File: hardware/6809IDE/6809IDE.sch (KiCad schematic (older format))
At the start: 5 parts, among them J1 SS50-LIKE, J2 ATA-IDE, J3 Conn_01x01

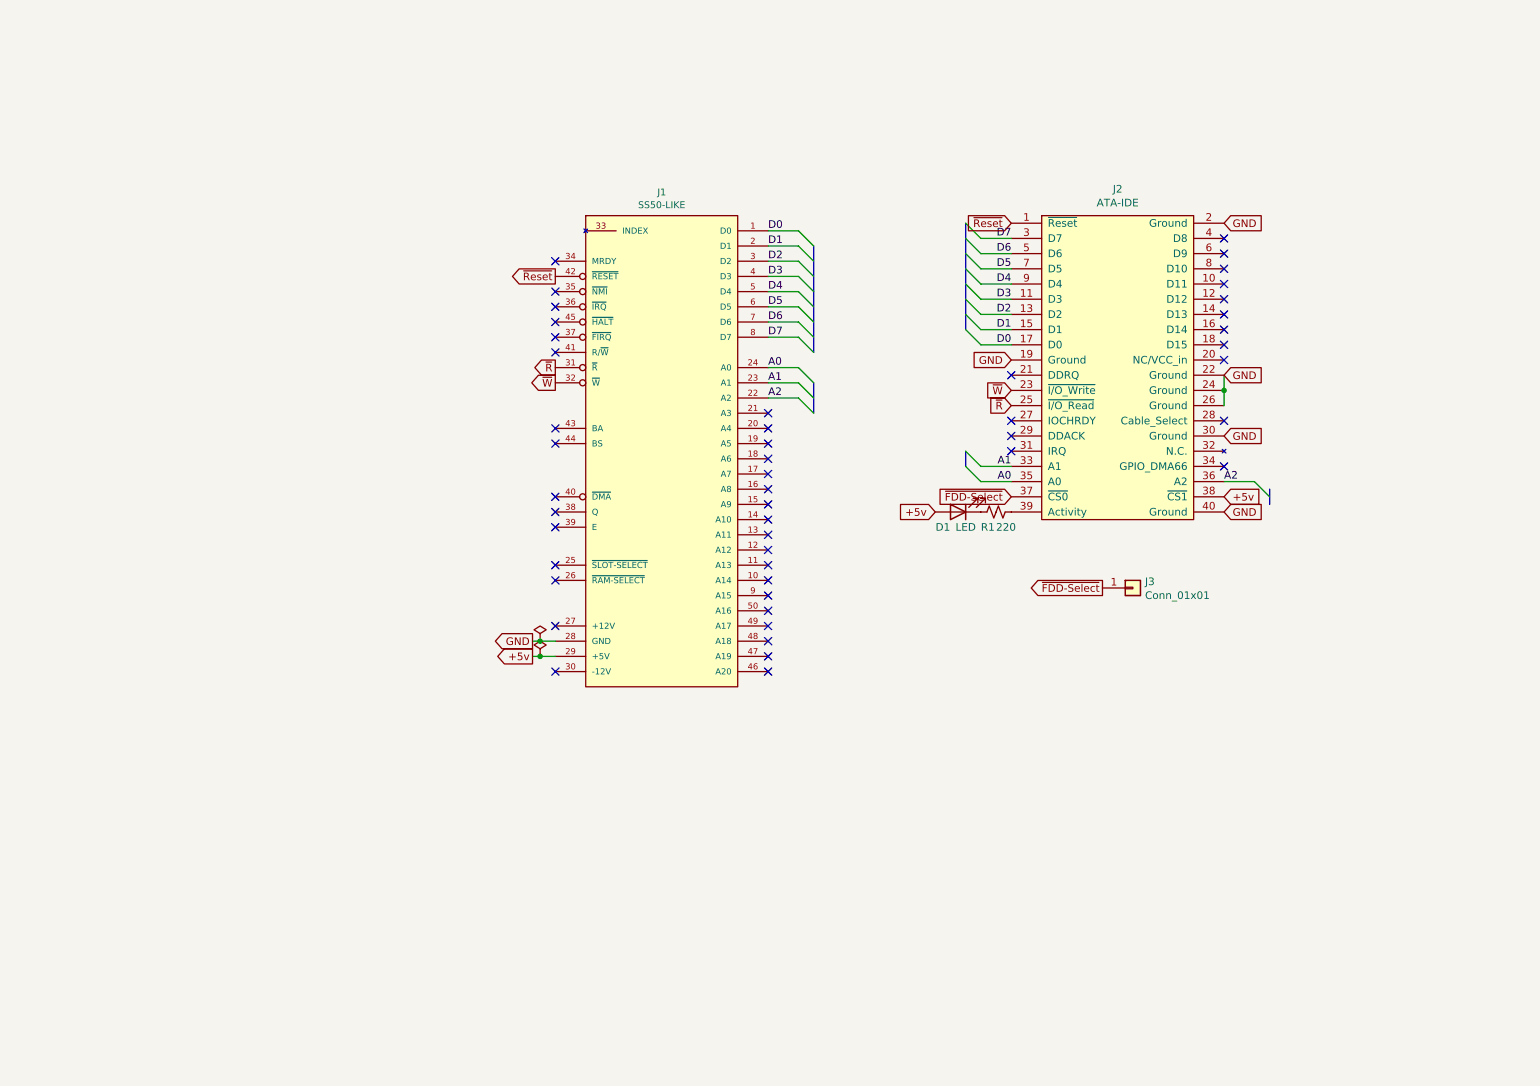
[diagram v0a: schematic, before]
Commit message: added latches
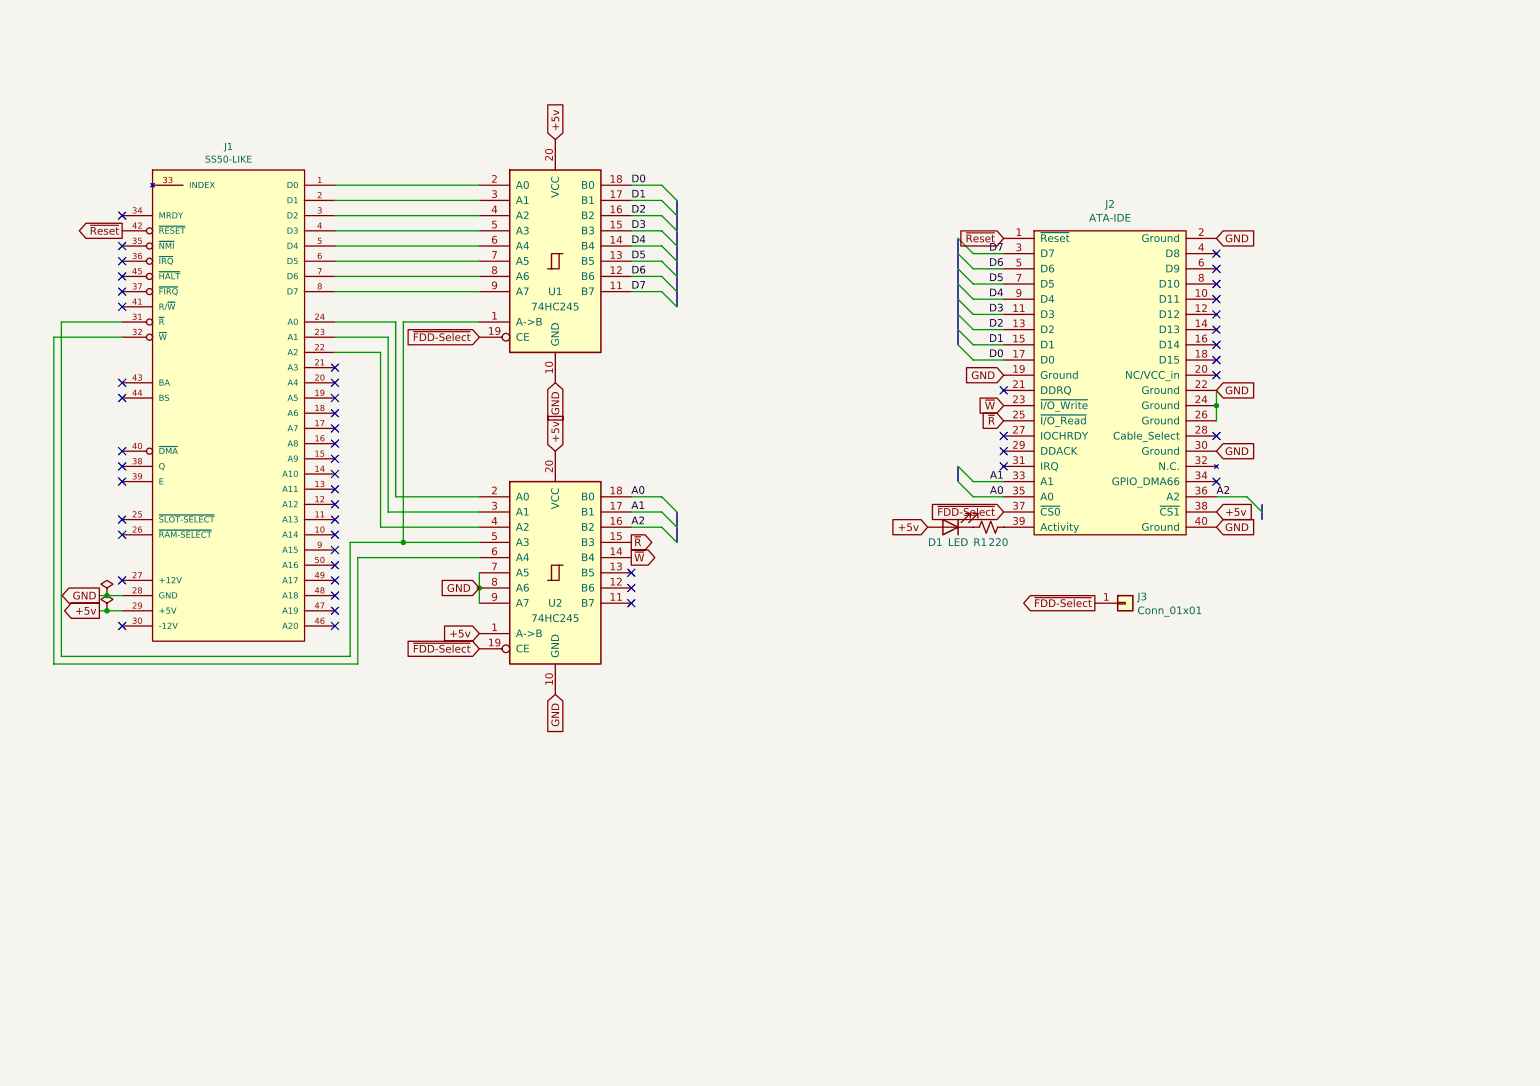
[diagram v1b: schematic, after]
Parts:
- added U1, U2: 74HC245, symbol 74xx:74HC245
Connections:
- net +5v: now also U1.20 (VCC), U2.1 (A->B), U2.20 (VCC)
- net A0: now also U2.18 (B0); no longer J1.24 (A0)
- net A1: now also U2.17 (B1); no longer J1.23 (A1)
- net A2: now also U2.16 (B2); no longer J1.22 (A2)
- net D0: now also U1.18 (B0); no longer J1.1 (D0)
- net D1: now also U1.17 (B1); no longer J1.2 (D1)
- net D2: now also U1.16 (B2); no longer J1.3 (D2)
- net D3: now also U1.15 (B3); no longer J1.4 (D3)
- net D4: now also U1.14 (B4); no longer J1.5 (D4)
- net D5: now also U1.13 (B5); no longer J1.6 (D5)
- net D6: now also U1.12 (B6); no longer J1.7 (D6)
- net D7: now also U1.11 (B7); no longer J1.8 (D7)
- net GND: now also U1.10 (GND), U2.10 (GND), U2.7 (A5), U2.8 (A6), U2.9 (A7)
- net ~FDD-Select: now also U1.19 (CE), U2.19 (CE)
- net ~R: now also U2.15 (B3); no longer J1.31 (~R)
- net ~W: now also U2.14 (B4); no longer J1.32 (~W)
- new net: J1.1 (D0), U1.2 (A0)
- new net: J1.2 (D1), U1.3 (A1)
- new net: J1.22 (A2), U2.4 (A2)
- new net: J1.23 (A1), U2.3 (A1)
- new net: J1.24 (A0), U2.2 (A0)
- new net: J1.3 (D2), U1.4 (A2)
- new net: J1.31 (~R), U1.1 (A->B), U2.5 (A3)
- new net: J1.32 (~W), U2.6 (A4)
- new net: J1.4 (D3), U1.5 (A3)
- new net: J1.5 (D4), U1.6 (A4)
- new net: J1.6 (D5), U1.7 (A5)
- new net: J1.7 (D6), U1.8 (A6)
- new net: J1.8 (D7), U1.9 (A7)
- no-connect marks 48 -> 51
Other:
- moved on the sheet: D1, J1, J2, J3, R1

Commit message: IDE controller
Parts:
- removed J2: ATA-IDE, symbol aspt:ATA-IDE
- added C1, C2: 0.1uF, Capacitor_THT:C_Disc_D5.0mm_W2.5mm_P5.00mm, symbol Device:C
- added D2, D3, D4: LED, LED_THT:LED_D5.0mm, symbol Device:LED
- added H1, H2, H3, H4: MountingHole, MountingHole:MountingHole_3.2mm_M3_ISO14580_Pad, symbol Mechanical:MountingHole
- added J3: Drive 1, Connector_PinHeader_2.54mm:PinHeader_2x20_P2.54mm_Vertical, symbol aspt:ATA-IDE
- added J4: Drive 2, Connector_PinHeader_2.54mm:PinHeader_2x20_P2.54mm_Vertical, symbol aspt:ATA-IDE
- added J5: Drive 2, Connector_PinHeader_2.00mm:PinHeader_2x22_P2.00mm_Vertical, symbol aspt:ATA-IDE-44
- added J6: Drive 1, Connector_PinHeader_2.00mm:PinHeader_2x22_P2.00mm_Vertical, symbol aspt:ATA-IDE-44
- added Logo1: Pinnated, Pinnated:Pinnule, symbol aspt:Pinnated
- added R2, R3, R4: 220, Resistor_THT:R_Axial_DIN0309_L9.0mm_D3.2mm_P12.70mm_Horizontal, symbol Device:R_Small_US
- D1: footprint (none) -> LED_THT:LED_D5.0mm
- J1: footprint SS-50_SS-50_BOARD_CONNECTOR -> Connector_PinHeader_2.54mm:PinHeader_2x25_P2.54mm_Vertical
- J2: renamed from J3; value Conn_01x01 -> Mem Addr; footprint (none) -> Connector_PinHeader_2.54mm:PinHeader_1x01_P2.54mm_Vertical
- R1: footprint (none) -> Resistor_THT:R_Axial_DIN0309_L9.0mm_D3.2mm_P12.70mm_Horizontal
- U1, U2: footprint (none) -> Package_DIP:DIP-20_W7.62mm_LongPads
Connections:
- net +5v: now also C1.2, C2.2, D2.2 (A), D3.2 (A), D4.2 (A), J3.38 (~CS1), J4.38 (~CS1), J5.38 (~CS1), J5.41 (VCC), J5.42 (VCC), J6.38 (~CS1), J6.41 (VCC), J6.42 (VCC)
- net A0: now also J3.35 (A0), J4.35 (A0), J5.35 (A0), J6.35 (A0)
- net A1: now also J3.33 (A1), J4.33 (A1), J5.33 (A1), J6.33 (A1)
- net A2: now also J3.36 (A2), J4.36 (A2), J5.36 (A2), J6.36 (A2)
- net D0: now also J3.17 (D0), J4.17 (D0), J5.17 (D0), J6.17 (D0)
- net D1: now also J3.15 (D1), J4.15 (D1), J5.15 (D1), J6.15 (D1)
- net D2: now also J3.13 (D2), J4.13 (D2), J5.13 (D2), J6.13 (D2)
- net D3: now also J3.11 (D3), J4.11 (D3), J5.11 (D3), J6.11 (D3)
- net D4: now also J3.9 (D4), J4.9 (D4), J5.9 (D4), J6.9 (D4)
- net D5: now also J3.7 (D5), J4.7 (D5), J5.7 (D5), J6.7 (D5)
- net D6: now also J3.5 (D6), J4.5 (D6), J5.5 (D6), J6.5 (D6)
- net D7: now also J3.3 (D7), J4.3 (D7), J5.3 (D7), J6.3 (D7)
- net GND: now also C1.1, C2.1, J3.19 (Ground), J3.2 (Ground), J3.22 (Ground), J3.24 (Ground), J3.26 (Ground), J3.30 (Ground), J3.40 (Ground), J4.19 (Ground), J4.2 (Ground), J4.22 (Ground), J4.24 (Ground), J4.26 (Ground), J4.30 (Ground), J4.40 (Ground), J5.19 (Ground), J5.2 (Ground), J5.22 (Ground), J5.24 (Ground), J5.26 (Ground), J5.30 (Ground), J5.40 (Ground), J5.43 (GND), J5.44 (GND), J6.19 (Ground), J6.2 (Ground), J6.22 (Ground), J6.24 (Ground), J6.26 (Ground), J6.30 (Ground), J6.40 (Ground), J6.43 (GND), J6.44 (GND); no longer U2.7 (A5), U2.8 (A6), U2.9 (A7)
- net ~FDD-Select: now also J3.37 (~CS0), J4.37 (~CS0), J5.37 (~CS0), J6.37 (~CS0)
- net ~R: now also J3.25 (~I/O_Read), J4.25 (~I/O_Read), J5.25 (~I/O_Read), J6.25 (~I/O_Read)
- net ~Reset: now also J3.1 (~Reset), J4.1 (~Reset), J5.1 (~Reset), J6.1 (~Reset)
- net ~W: now also J3.23 (~I/O_Write), J4.23 (~I/O_Write), J5.23 (~I/O_Write), J6.23 (~I/O_Write)
- net at R1.1: now also J3.39 (Activity)
- new net: D2.1 (K), R2.2
- new net: J4.39 (Activity), R2.1
- new net: D3.1 (K), R3.2
- new net: J5.39 (Activity), R3.1
- new net: D4.1 (K), R4.2
- new net: J6.39 (Activity), R4.1
- no-connect marks 51 -> 99
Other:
- moved on the sheet: D1, J1, J2, R1, U1, U2

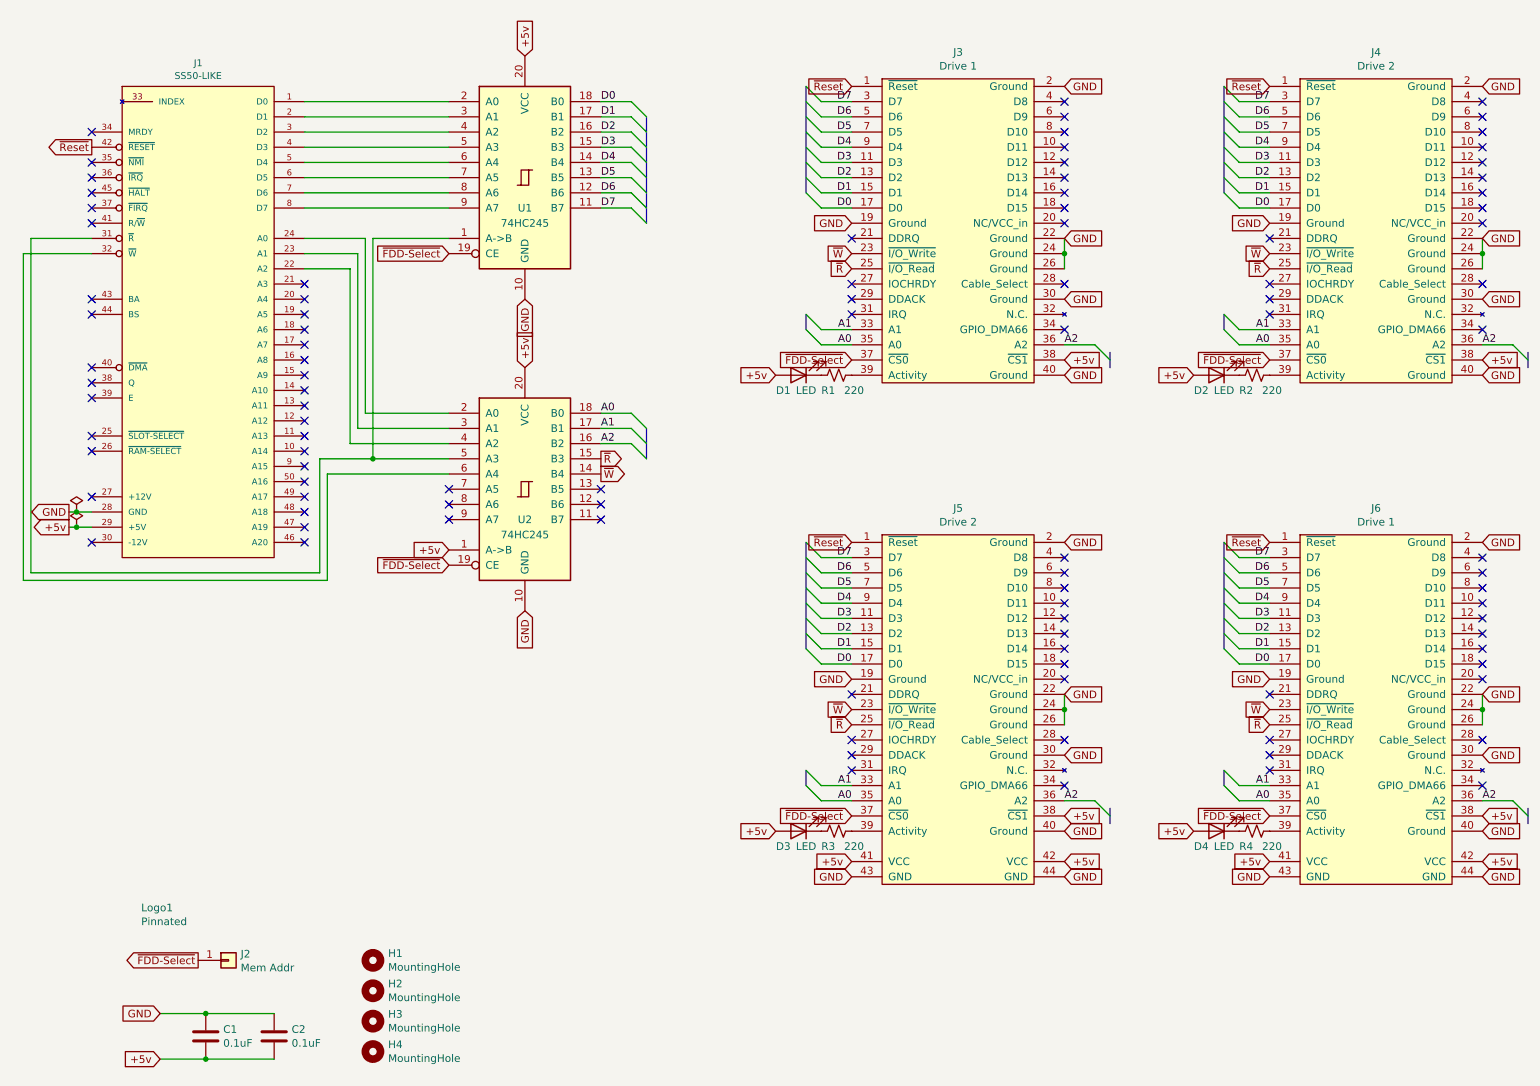
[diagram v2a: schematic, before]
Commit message: move to single connector
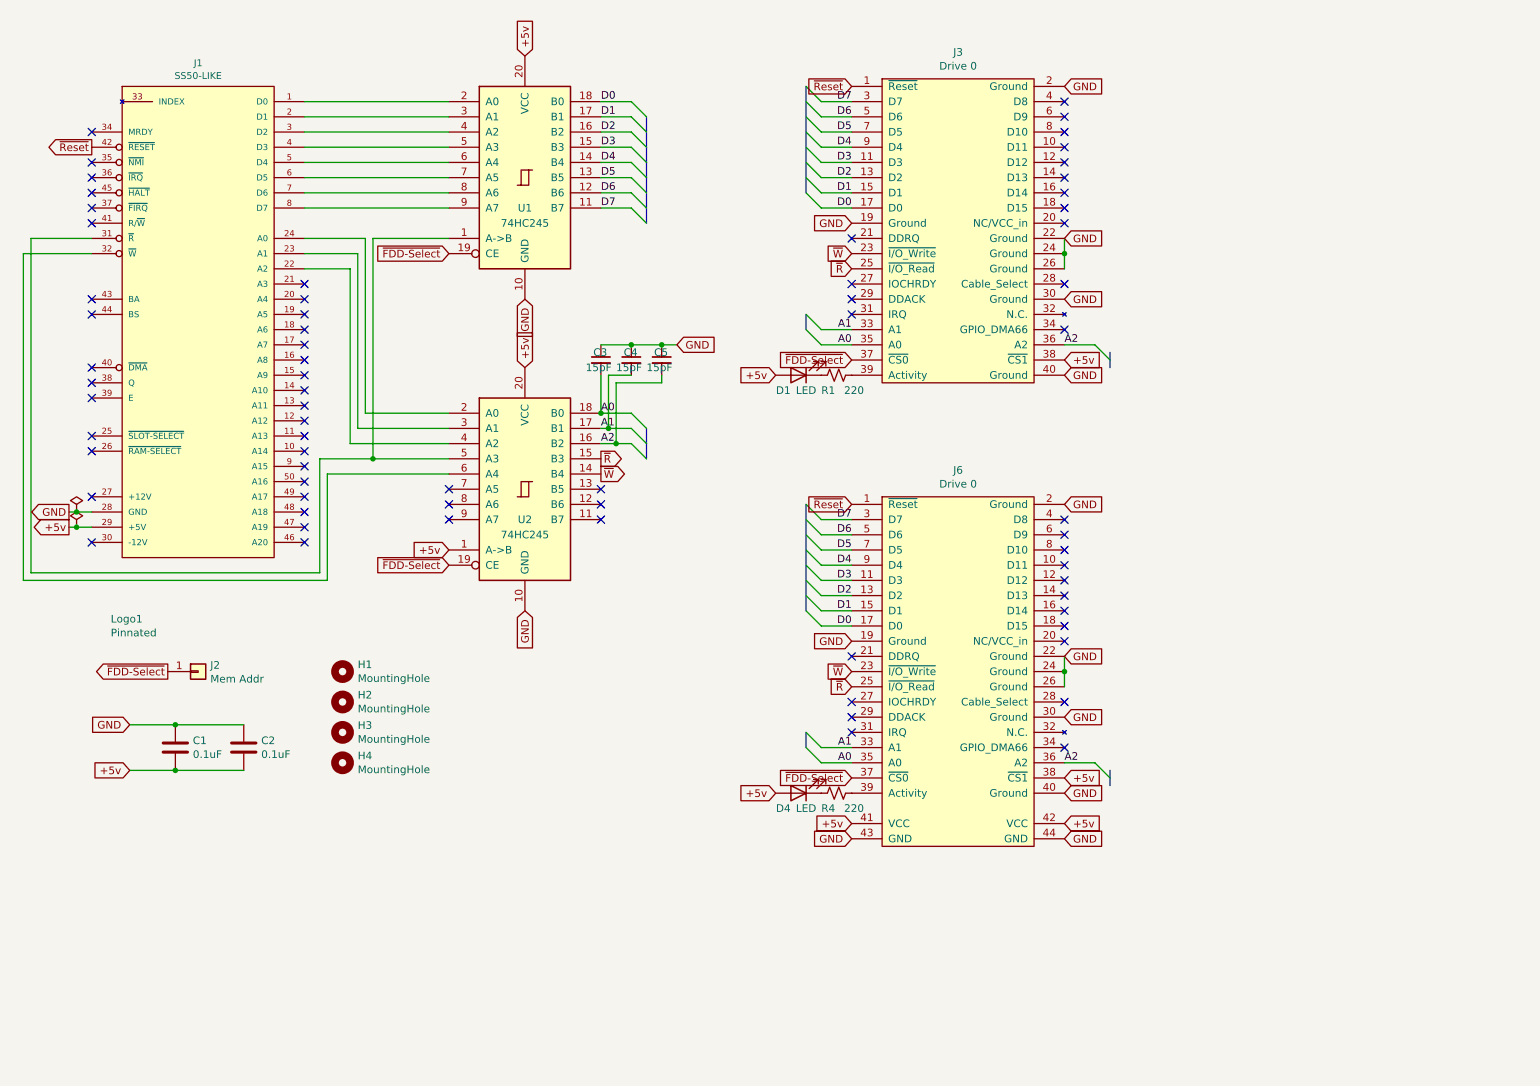
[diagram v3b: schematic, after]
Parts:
- removed D2, D3: LED, LED_THT:LED_D5.0mm, symbol Device:LED
- removed J4: Drive 2, Connector_PinHeader_2.54mm:PinHeader_2x20_P2.54mm_Vertical, symbol aspt:ATA-IDE
- removed J5: Drive 2, Connector_PinHeader_2.00mm:PinHeader_2x22_P2.00mm_Vertical, symbol aspt:ATA-IDE-44
- removed R2, R3: 220, Resistor_THT:R_Axial_DIN0309_L9.0mm_D3.2mm_P12.70mm_Horizontal, symbol Device:R_Small_US
- added C3, C4, C5: 15pF, Capacitor_THT:C_Disc_D5.0mm_W2.5mm_P2.50mm, symbol Device:C_Small
- J3, J6: value Drive 1 -> Drive 0
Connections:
- net A0: now also C3.2
- net A1: now also C4.2
- net A2: now also C5.2
- net GND: now also C3.1, C4.1, C5.1
- no-connect marks 99 -> 69
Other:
- moved on the sheet: C1, C2, D4, H1, H2, H3, H4, J2, J6, R4
